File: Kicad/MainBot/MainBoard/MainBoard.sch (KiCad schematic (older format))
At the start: 79 parts, among them J1 Conn_01x02, J10 Conn_01x24, J11 01x24, J12 Conn_01x05, J13 Conn_01x03, J14 Conn_01x03, J15 Conn_01x03, J16 01x04, J17 01x04, J18 01x04, J19 01x04, J20 Conn_01x03, U1 AZ1117-3.3, U2 TCA9548A, U3 Teensy3.6, U4 DRV8825, U5 DRV8825, U6 DRV8825, U7 DRV8825

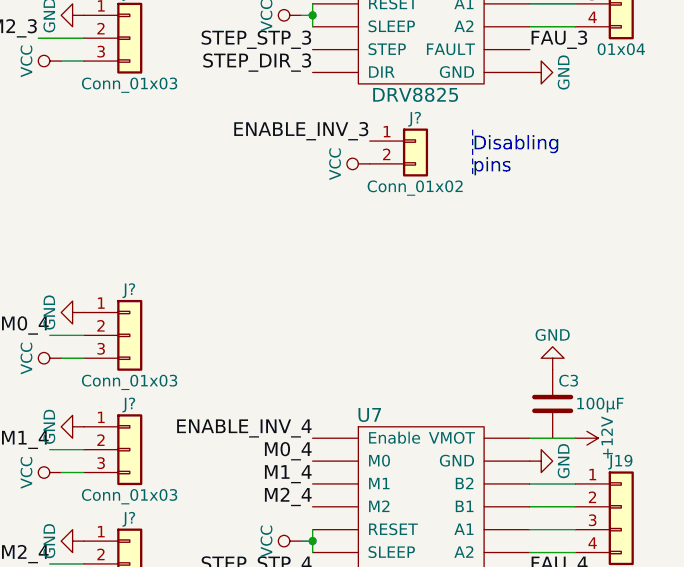
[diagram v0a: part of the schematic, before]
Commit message: Added external connectors to Steppers Fault pins
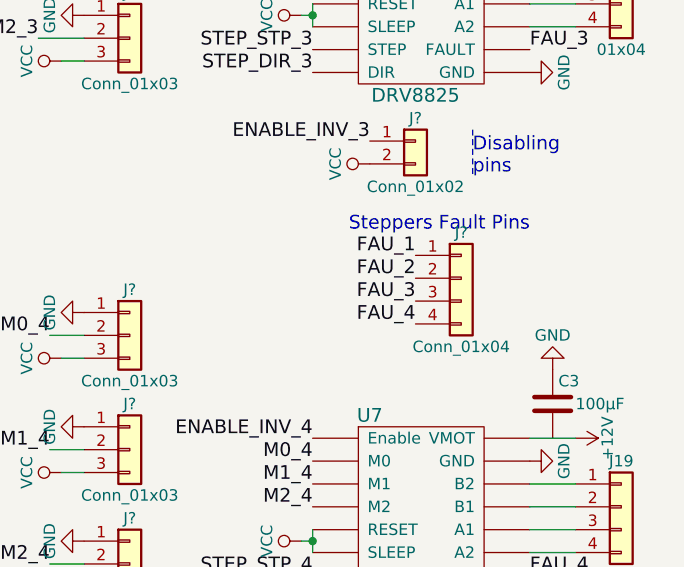
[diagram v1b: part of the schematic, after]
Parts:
- added J?: Conn_01x04, symbol Conn_01x04
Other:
- note added: "Steppers Fault Pins\n"
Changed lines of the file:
@@
 Connection ~ 6200 5200
 Connection ~ 6200 5300
+$Comp
+L Conn_01x04 J?
+U 1 1 5C79CEF9
+P 15200 6700
+F 0 "J?" H 15200 6900 50  0000 C CNN
+F 1 "Conn_01x04" H 15200 6400 50  0000 C CNN
+F 2 "" H 15200 6700 50  0001 C CNN
+F 3 "" H 15200 6700 50  0001 C CNN
+	1    15200 6700
+	1    0    0    -1
+$EndComp
+Text Label 15000 6600 2    60   ~ 0
+FAU_1
+Text Label 15000 6700 2    60   ~ 0
+FAU_2
+Text Label 15000 6800 2    60   ~ 0
+FAU_3
+Text Label 15000 6900 2    60   ~ 0
+FAU_4
+Text Notes 15500 6500 2    60   ~ 0
+Steppers Fault Pins\n
 $EndSCHEMATC

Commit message: Added DAC0 and DAC1 labels
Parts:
- removed Q?: 2N7000, TO_SOT_Packages_THT:TO-92_Molded_Narrow, symbol 2N7000
- added D?: LED, symbol LED
- added R?: R, symbol R
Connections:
- wire segments 168 -> 170
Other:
- note added: "Debug 1\n"
- note added: "Debug 2\n"
- note added: "Dynamixel\n"
- note removed: "Ajouter canal multiple I2C au cas où\n"
- note removed: "Dynamixel ?\n"
- note removed: "Nettoyage des noms des nets\n"
- note removed: "Test LED RGB -> Driver Transistor\n"
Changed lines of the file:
@@
 P 5950 7200
 F 0 "J10" H 5950 8400 50  0000 C CNN
-F 1 "Conn_01x24" H 5950 5900 50  0000 C CNN
+F 1 "Conn_01x24" H 5800 5900 50  0000 C CNN
 F 2 "Pin_Headers:Pin_Header_Straight_1x24_Pitch2.54mm" H 5950 7200 50  0001 C CNN
 F 3 "" H 5950 7200 50  0001 C CNN
@@
 Text Label 850  9400 0    60   ~ 0
 3.3V
-Text Notes 4200 1400 0    60   ~ 0
-Test LED RGB -> Driver Transistor\n
 $Comp
 L GND #PWR?
@@
 P 5650 7200
 F 0 "J?" H 5650 8400 50  0000 C CNN
-F 1 "Conn_01x24" H 5650 5900 50  0000 C CNN
+F 1 "Conn_01x24" H 5800 5900 50  0000 C CNN
 F 2 "Pin_Headers:Pin_Header_Straight_1x24_Pitch2.54mm" H 5650 7200 50  0001 C CNN
 F 3 "" H 5650 7200 50  0001 C CNN
@@
 Text Label 950  2800 2    60   ~ 0
 ADDR_2
-Text Notes 4200 1500 0    60   ~ 0
-Ajouter canal multiple I2C au cas où\n
-Text Notes 4200 1600 0    60   ~ 0
-Dynamixel ?\n
-Text Notes 4200 1700 0    60   ~ 0
-Nettoyage des noms des nets\n
 $Comp
 L Conn_02x04_Counter_Clockwise J?
@@
 	1    14500 7850
 	0    -1   -1   0
-$EndComp
-$Comp
-L 2N7000 Q?
-U 1 1 5C782DAB
-P 6200 1350
-F 0 "Q?" H 6400 1425 50  0000 L CNN
-F 1 "2N7000" H 6400 1350 50  0000 L CNN
-F 2 "TO_SOT_Packages_THT:TO-92_Molded_Narrow" H 6400 1275 50  0001 L CIN
-F 3 "" H 6200 1350 50  0001 L CNN
-	1    6200 1350
-	1    0    0    -1
 $EndComp
 $Comp
@@
 Text Notes 15500 6500 2    60   ~ 0
 Steppers Fault Pins\n
+Text Notes 4050 2950 2    60   ~ 0
+Debug 1\n
+Text Notes 4050 3400 2    60   ~ 0
+Debug 2\n
+$Comp
+L LED D?
+U 1 1 5C7A0281
+P 3800 3550
+F 0 "D?" H 3800 3650 50  0000 C CNN
+F 1 "LED" H 3800 3450 50  0000 C CNN
+F 2 "" H 3800 3550 50  0001 C CNN
+F 3 "" H 3800 3550 50  0001 C CNN
+	1    3800 3550
+	1    0    0    -1
+$EndComp
+$Comp
+L R R?
+U 1 1 5C7A0287
+P 4150 3550
+F 0 "R?" V 4230 3550 50  0000 C CNN
+F 1 "R" V 4150 3550 50  0000 C CNN
+F 2 "" V 4080 3550 50  0001 C CNN
+F 3 "" H 4150 3550 50  0001 C CNN
+	1    4150 3550
+	0    1    1    0
+$EndComp
+$Comp
+L GND #PWR?
+U 1 1 5C7A028D
+P 3600 3550
+F 0 "#PWR?" H 3600 3300 50  0001 C CNN
+F 1 "GND" H 3600 3400 50  0000 C CNN
+F 2 "" H 3600 3550 50  0001 C CNN
+F 3 "" H 3600 3550 50  0001 C CNN
+	1    3600 3550
+	0    1    1    0
+$EndComp
+Wire Wire Line
+	3600 3550 3650 3550
+Wire Wire Line
+	3950 3550 4000 3550
+Text Notes 5300 2650 2    60   ~ 0
+Dynamixel\n
+Text Label 6950 6700 2    60   ~ 0
+DAC0
+Text Label 6950 6800 2    60   ~ 0
+DAC1
 $EndSCHEMATC

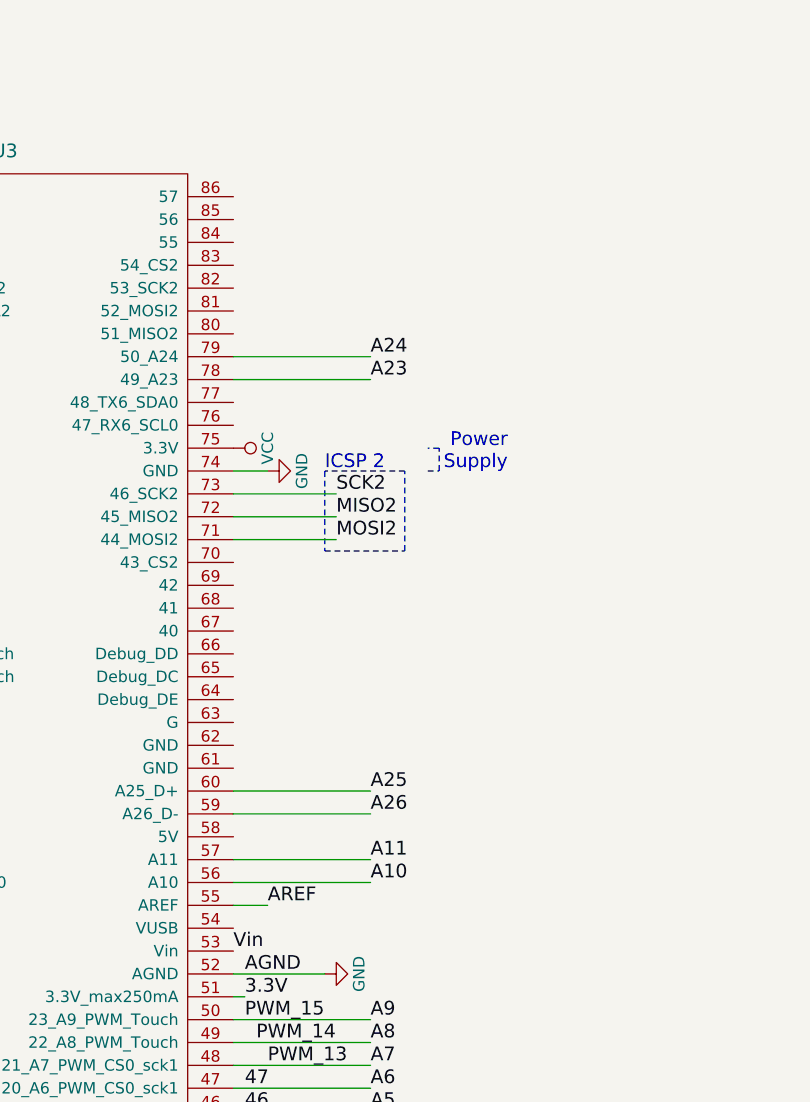
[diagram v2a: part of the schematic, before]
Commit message: Connected backside pins to headers
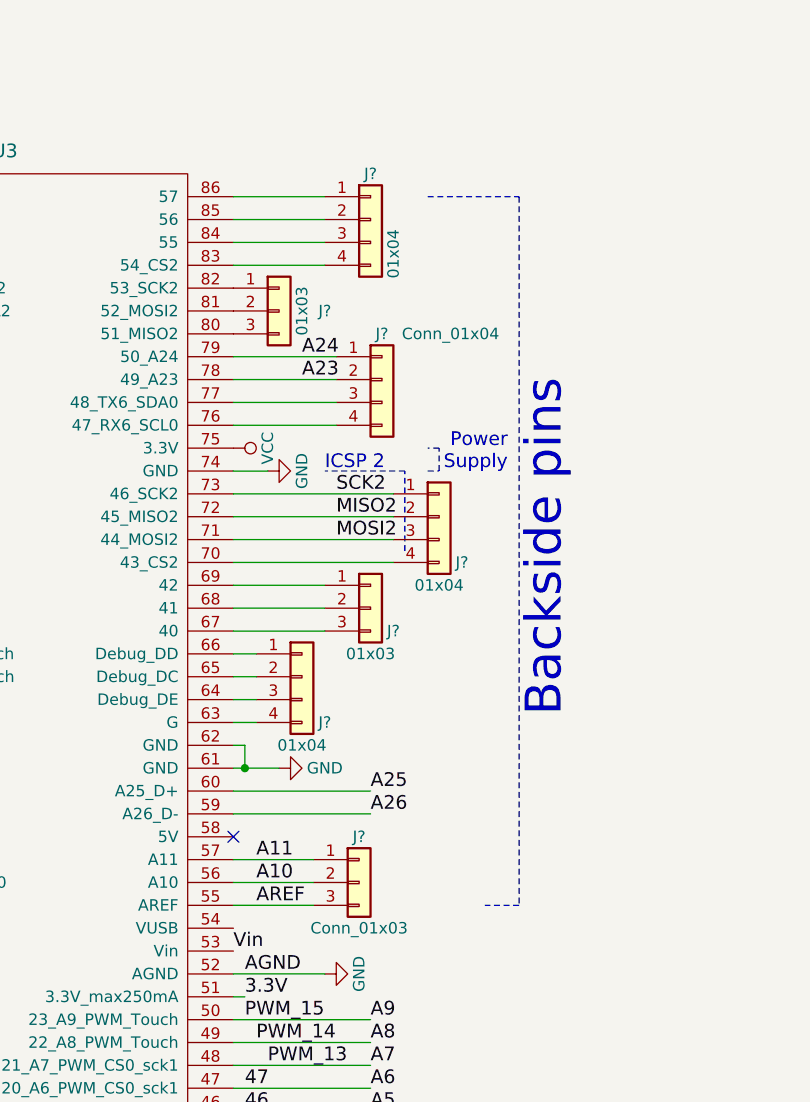
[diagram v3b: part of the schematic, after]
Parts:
- added J? (x3): 01x04, symbol Conn_01x04
- added J? (x2): 01x03, symbol Conn_01x03
- added J?: Conn_01x04, symbol Conn_01x04
- added J?: Conn_01x03, symbol Conn_01x03
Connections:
- net A10: now also J?.2 (Pin_2)
- net A11: now also J?.1 (Pin_1)
- net A23: now also J?.2 (Pin_2)
- net A24: now also J?.1 (Pin_1)
- net AREF: now also J?.3 (Pin_3)
- net GND: now also U3.61 (GND), U3.62 (GND)
- net MISO2: now also J?.2 (Pin_2)
- net MOSI2: now also J?.3 (Pin_3)
- net SCK2: now also J?.1 (Pin_1)
- net at U3.63 (G): now also J?.4 (Pin_4)
- net at U3.64 (Debug_DE): now also J?.3 (Pin_3)
- net at U3.65 (Debug_DC): now also J?.2 (Pin_2)
- net at U3.66 (Debug_DD): now also J?.1 (Pin_1)
- net at U3.67 (40): now also J?.3 (Pin_3)
- net at U3.68 (41): now also J?.2 (Pin_2)
- net at U3.69 (42): now also J?.1 (Pin_1)
- net at U3.70 (43_CS2): now also J?.4 (Pin_4)
- net at U3.76 (47_RX6_SCL0): now also J?.4 (Pin_4)
- net at U3.77 (48_TX6_SDA0): now also J?.3 (Pin_3)
- net at U3.80 (51_MISO2): now also J?.3 (Pin_3)
- net at U3.81 (52_MOSI2): now also J?.2 (Pin_2)
- net at U3.82 (53_SCK2): now also J?.1 (Pin_1)
- net at U3.83 (54_CS2): now also J?.4 (Pin_4)
- net at U3.84 (55): now also J?.3 (Pin_3)
- net at U3.85 (56): now also J?.2 (Pin_2)
- net at U3.86 (57): now also J?.1 (Pin_1)
- no-connect marks 3 -> 4
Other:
- note added: "Backside pins"
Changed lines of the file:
@@
 	750  9400 850  9400
 Wire Wire Line
-	9300 4400 9750 4400
-Wire Wire Line
-	9300 4500 9750 4500
-Wire Wire Line
-	9300 4600 9750 4600
-Wire Notes Line
-	9700 4300 9700 4650
-Wire Notes Line
-	9700 4650 10050 4650
+	9300 4400 10000 4400
+Wire Wire Line
+	9300 4500 10000 4500
+Wire Wire Line
+	9300 4600 10000 4600
 Wire Notes Line
 	10050 4650 10050 4300
@@
 Text Label 9900 7300 0    60   ~ 0
 A3
-Text Label 9900 6100 0    60   ~ 0
+Text Label 9400 6100 0    60   ~ 0
 A10
-Text Label 9900 6000 0    60   ~ 0
+Text Label 9400 6000 0    60   ~ 0
 A11
 Text Label 9900 5800 0    60   ~ 0
@@
 Text Label 9900 5700 0    60   ~ 0
 A25
-Text Label 9900 3900 0    60   ~ 0
+Text Label 9600 3900 0    60   ~ 0
 A23
-Text Label 9900 3800 0    60   ~ 0
+Text Label 9600 3800 0    60   ~ 0
 A24
 Wire Wire Line
-	9900 3800 9300 3800
-Wire Wire Line
-	9300 3900 9900 3900
-Wire Wire Line
 	9900 5700 9300 5700
 Wire Wire Line
 	9900 5800 9300 5800
-Wire Wire Line
-	9900 6000 9300 6000
-Wire Wire Line
-	9300 6100 9900 6100
 $Comp
 L Conn_01x02 J?
@@
 Text Notes 15150 8550 0    60   ~ 0
 Disabling\npins
-Wire Wire Line
-	9300 6200 9450 6200
-Text Label 9450 6200 0    60   ~ 0
+Text Label 9400 6200 0    60   ~ 0
 AREF
 $Comp
@@
 Text Label 6950 6800 2    60   ~ 0
 DAC1
+$Comp
+L Conn_01x04 J?
+U 1 1 5C7AE056
+P 9600 5200
+F 0 "J?" H 9700 5000 50  0000 C CNN
+F 1 "01x04" H 9600 4900 50  0000 C CNN
+F 2 "" H 9600 5200 50  0001 C CNN
+F 3 "" H 9600 5200 50  0001 C CNN
+	1    9600 5200
+	1    0    0    -1
+$EndComp
+Wire Wire Line
+	9300 5100 9400 5100
+Wire Wire Line
+	9400 5200 9300 5200
+Wire Wire Line
+	9300 5300 9400 5300
+Wire Wire Line
+	9300 5400 9400 5400
+$Comp
+L Conn_01x03 J?
+U 1 1 5C7AE844
+P 9900 4900
+F 0 "J?" H 10000 4800 50  0000 C CNN
+F 1 "01x03" H 9900 4700 50  0000 C CNN
+F 2 "" H 9900 4900 50  0001 C CNN
+F 3 "" H 9900 4900 50  0001 C CNN
+	1    9900 4900
+	1    0    0    -1
+$EndComp
+Wire Wire Line
+	9300 4800 9700 4800
+Wire Wire Line
+	9700 4900 9300 4900
+Wire Wire Line
+	9300 5000 9700 5000
+$Comp
+L Conn_01x04 J?
+U 1 1 5C7B11E6
+P 10200 4500
+F 0 "J?" H 10300 4300 50  0000 C CNN
+F 1 "01x04" H 10200 4200 50  0000 C CNN
+F 2 "" H 10200 4500 50  0001 C CNN
+F 3 "" H 10200 4500 50  0001 C CNN
+	1    10200 4500
+	1    0    0    -1
+$EndComp
+Wire Wire Line
+	10000 4700 9300 4700
+$Comp
+L Conn_01x04 J?
+U 1 1 5C7B2782
+P 9950 3900
+F 0 "J?" H 9950 4100 50  0000 C CNN
+F 1 "Conn_01x04" H 10250 4100 50  0000 C CNN
+F 2 "" H 9950 3900 50  0001 C CNN
+F 3 "" H 9950 3900 50  0001 C CNN
+	1    9950 3900
+	1    0    0    -1
+$EndComp
+Wire Wire Line
+	9300 4100 9750 4100
+Wire Wire Line
+	9750 4000 9300 4000
+Wire Wire Line
+	9300 3900 9750 3900
+Wire Wire Line
+	9750 3800 9300 3800
+$Comp
+L Conn_01x03 J?
+U 1 1 5C7B4394
+P 9500 3600
+F 0 "J?" H 9700 3600 50  0000 C CNN
+F 1 "01x03" V 9600 3600 50  0000 C CNN
+F 2 "" H 9500 3600 50  0001 C CNN
+F 3 "" H 9500 3600 50  0001 C CNN
+	1    9500 3600
+	1    0    0    -1
+$EndComp
+$Comp
+L Conn_01x04 J?
+U 1 1 5C7B4A77
+P 9900 3200
+F 0 "J?" H 9900 3400 50  0000 C CNN
+F 1 "01x04" V 10000 3050 50  0000 C CNN
+F 2 "" H 9900 3200 50  0001 C CNN
+F 3 "" H 9900 3200 50  0001 C CNN
+	1    9900 3200
+	1    0    0    -1
+$EndComp
+Wire Wire Line
+	9300 3400 9700 3400
+Wire Wire Line
+	9700 3300 9300 3300
+Wire Wire Line
+	9300 3200 9700 3200
+Wire Wire Line
+	9700 3100 9300 3100
+$Comp
+L Conn_01x03 J?
+U 1 1 5C7B57B2
+P 9850 6100
+F 0 "J?" H 9850 6300 50  0000 C CNN
+F 1 "Conn_01x03" H 9850 5900 50  0000 C CNN
+F 2 "" H 9850 6100 50  0001 C CNN
+F 3 "" H 9850 6100 50  0001 C CNN
+	1    9850 6100
+	1    0    0    -1
+$EndComp
+Wire Wire Line
+	9650 6000 9300 6000
+Wire Wire Line
+	9300 6100 9650 6100
+Wire Wire Line
+	9650 6200 9300 6200
+Wire Wire Line
+	9300 5500 9350 5500
+Wire Wire Line
+	9350 5500 9350 5600
+Wire Wire Line
+	9300 5600 9500 5600
+$Comp
+L GND #PWR?
+U 1 1 5C7B6E99
+P 9500 5600
+F 0 "#PWR?" H 9500 5350 50  0001 C CNN
+F 1 "GND" V 9500 5400 50  0000 C CNN
+F 2 "" H 9500 5600 50  0001 C CNN
+F 3 "" H 9500 5600 50  0001 C CNN
+	1    9500 5600
+	0    -1   -1   0
+$EndComp
+Connection ~ 9350 5600
+Wire Notes Line
+	10150 3100 10550 3100
+Wire Notes Line
+	10550 3100 10550 6200
+Wire Notes Line
+	10550 6200 10400 6200
+Text Notes 10750 3900 3    157  ~ 0
+Backside pins
+NoConn ~ 9300 5900
 $EndSCHEMATC

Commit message: Added notes
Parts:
- added J?: 01x02, symbol Conn_01x02
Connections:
- net Vin: now also J?.1 (Pin_1), J?.2 (Pin_2)
- no-connect marks 4 -> 5
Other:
- note added: "No 5V power supply: NC\n"
- note added: "No use: NC"
- note added: "Optional connections to AREF\n"
- note added: "Vin requires at least 3.6V, \nmore than regulator output:\n optional Not Connect"
- note removed: "Power \nSupply\n"
- moved on the sheet: J?
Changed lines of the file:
@@
 encoding utf-8
 Sheet 1 1
-Title "MainBot PCB by Arnaud Schlumberger"
-Date "2019-02-02"
-Rev "2"
+Title "MainBot Motherboardby Arnaud Schlumberger"
+Date "2019-03-01"
+Rev "1"
 Comp "Robot Télécom Strasbourg"
 Comment1 ""
@@
 	0    -1   -1   0
 $EndComp
-Text Label 6500 4500 0    60   ~ 0
-3.3V
-Text Label 7300 4500 2    60   ~ 0
-3.3V
 Text Label 850  9400 0    60   ~ 0
 3.3V
@@
 L Conn_01x03 J?
 U 1 1 5C7019BF
-P 11400 10850
-F 0 "J?" H 11400 11050 50  0000 C CNN
-F 1 "Conn_01x03" H 11400 10650 50  0000 C CNN
-F 2 "" H 11400 10850 50  0001 C CNN
-F 3 "" H 11400 10850 50  0001 C CNN
-	1    11400 10850
+P 11350 6000
+F 0 "J?" H 11350 6200 50  0000 C CNN
+F 1 "Conn_01x03" H 11350 5800 50  0000 C CNN
+F 2 "" H 11350 6000 50  0001 C CNN
+F 3 "" H 11350 6000 50  0001 C CNN
+	1    11350 6000
 	1    0    0    -1
 $EndComp
-Text Label 11200 10850 2    60   ~ 0
+Text Label 11150 6000 2    60   ~ 0
 AREF
 $Comp
 L VCC #PWR?
 U 1 1 5C702C85
-P 11100 10750
-F 0 "#PWR?" H 11100 10600 50  0001 C CNN
-F 1 "VCC" H 11100 10900 50  0000 C CNN
-F 2 "" H 11100 10750 50  0001 C CNN
-F 3 "" H 11100 10750 50  0001 C CNN
-	1    11100 10750
+P 11050 5900
+F 0 "#PWR?" H 11050 5750 50  0001 C CNN
+F 1 "VCC" H 11050 6050 50  0000 C CNN
+F 2 "" H 11050 5900 50  0001 C CNN
+F 3 "" H 11050 5900 50  0001 C CNN
+	1    11050 5900
 	0    -1   -1   0
 $EndComp
@@
 L GND #PWR?
 U 1 1 5C702D2D
-P 11100 10950
-F 0 "#PWR?" H 11100 10700 50  0001 C CNN
-F 1 "GND" H 11100 10800 50  0000 C CNN
-F 2 "" H 11100 10950 50  0001 C CNN
-F 3 "" H 11100 10950 50  0001 C CNN
-	1    11100 10950
+P 11050 6100
+F 0 "#PWR?" H 11050 5850 50  0001 C CNN
+F 1 "GND" H 11050 5950 50  0000 C CNN
+F 2 "" H 11050 6100 50  0001 C CNN
+F 3 "" H 11050 6100 50  0001 C CNN
+	1    11050 6100
 	0    1    1    0
 $EndComp
 Wire Wire Line
-	11200 10750 11100 10750
+	11150 5900 11050 5900
 Wire Wire Line
-	11200 10950 11100 10950
+	11150 6100 11050 6100
 $Comp
 L GND #PWR?
@@
 Text Label 9300 6400 0    60   ~ 0
 Vin
-Wire Notes Line
-	10150 4300 10200 4300
-Wire Notes Line
-	10200 4300 10200 4200
-Wire Notes Line
-	10200 4200 10150 4200
-Text Notes 10500 4300 2    60   ~ 0
-Power \nSupply\n
 Wire Wire Line
 	14550 7800 14550 7900
@@
 Backside pins
 NoConn ~ 9300 5900
+$Comp
+L VCC #PWR?
+U 1 1 5C7BED09
+P 6500 4500
+F 0 "#PWR?" H 6500 4350 50  0001 C CNN
+F 1 "VCC" H 6500 4650 50  0000 C CNN
+F 2 "" H 6500 4500 50  0001 C CNN
+F 3 "" H 6500 4500 50  0001 C CNN
+	1    6500 4500
+	0    1    1    0
+$EndComp
+$Comp
+L VCC #PWR?
+U 1 1 5C7BEDCD
+P 7300 4500
+F 0 "#PWR?" H 7300 4350 50  0001 C CNN
+F 1 "VCC" H 7300 4650 50  0000 C CNN
+F 2 "" H 7300 4500 50  0001 C CNN
+F 3 "" H 7300 4500 50  0001 C CNN
+	1    7300 4500
+	0    -1   -1   0
+$EndComp
+$Comp
+L Conn_01x02 J?
+U 1 1 5C7C06FB
+P 10400 6400
+F 0 "J?" H 10400 6500 50  0000 C CNN
+F 1 "01x02" H 10400 6200 50  0000 C CNN
+F 2 "" H 10400 6400 50  0001 C CNN
+F 3 "" H 10400 6400 50  0001 C CNN
+	1    10400 6400
+	1    0    0    -1
+$EndComp
+Wire Wire Line
+	9300 6400 10200 6400
+Wire Wire Line
+	10150 6400 10150 6500
+Wire Wire Line
+	10150 6500 10200 6500
+Connection ~ 10150 6400
+Text Notes 11300 6550 2    39   ~ 0
+Vin requires at least 3.6V, \nmore than regulator output:\n optional Not Connect
+NoConn ~ 9300 6300
+Text Notes 12300 6000 2    39   ~ 0
+Optional connections to AREF\n
+Text Notes 9700 5900 2    20   ~ 0
+No 5V power supply: NC\n
+Text Notes 9500 6300 2    20   ~ 0
+No use: NC
 $EndSCHEMATC
